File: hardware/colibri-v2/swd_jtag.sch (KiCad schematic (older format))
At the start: 10 parts

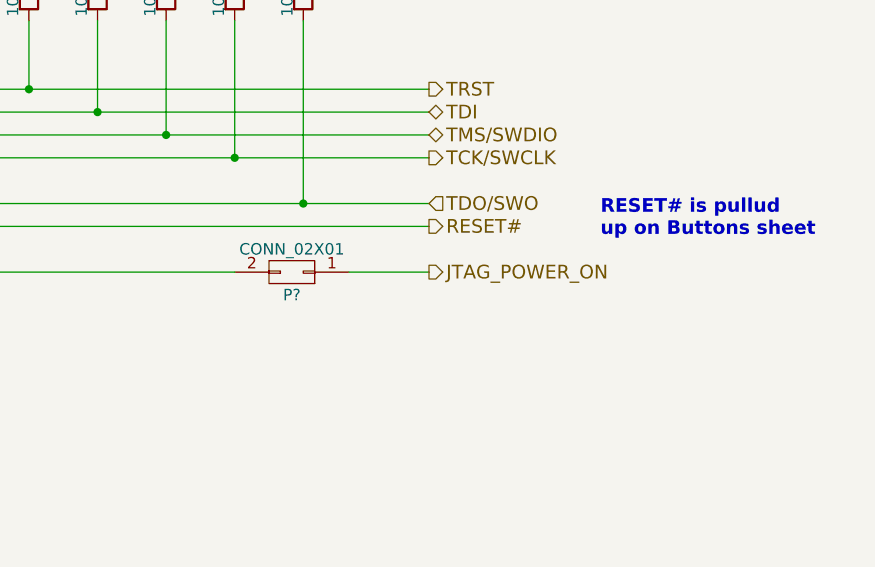
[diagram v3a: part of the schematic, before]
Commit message: Work on cortex,jtag,buttons sheets
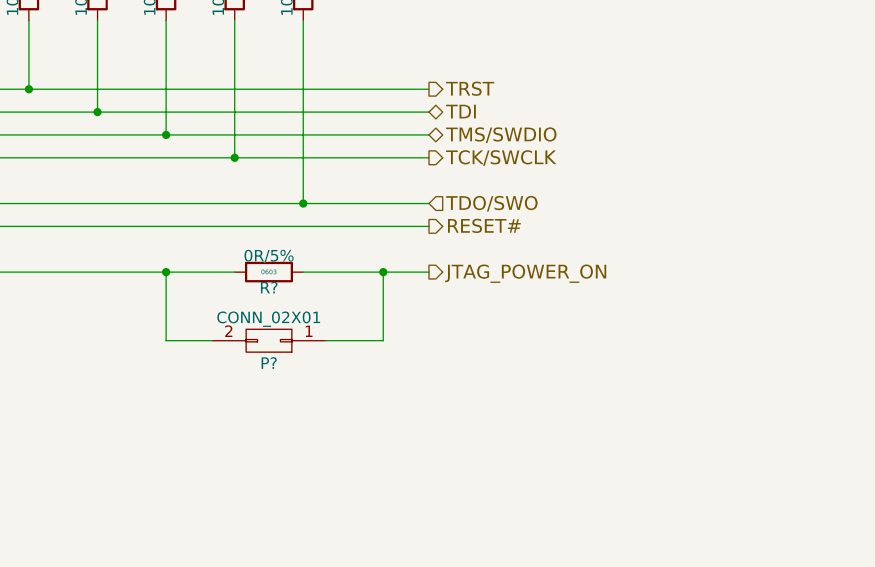
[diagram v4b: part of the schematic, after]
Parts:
- added R?: 0R/5%, Resistors_SMD:R_0603, symbol R_SMT
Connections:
- net JTAG_POWER: now also R?.2
- net JTAG_POWER_ON: now also R?.1
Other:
- note removed: "RESET# is pullud \nup on Buttons sheet"
- moved on the sheet: P?
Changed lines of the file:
@@
 L CONN_02X01 P?
 U 1 1 55768A67
-P 7900 2800
-F 0 "P?" H 7900 2900 50  0000 C CNN
-F 1 "CONN_02X01" H 7900 2700 50  0000 C CNN
-F 2 "" H 7900 1600 60  0001 C CNN
-F 3 "" H 7900 1600 60  0000 C CNN
-	1    7900 2800
+P 7800 3100
+F 0 "P?" H 7800 3200 50  0000 C CNN
+F 1 "CONN_02X01" H 7800 3000 50  0000 C CNN
+F 2 "" H 7800 1900 60  0001 C CNN
+F 3 "" H 7800 1900 60  0000 C CNN
+	1    7800 3100
 	-1   0    0    1
 $EndComp
@@
 	5600 2700 5900 2700
 Wire Wire Line
-	8150 2800 8500 2800
+	7950 2800 8500 2800
 Wire Wire Line
 	3300 1200 7950 1200
@@
 Wire Wire Line
 	4000 5000 4950 5000
-Text Notes 9250 2650 0    60   ~ 12
-RESET# is pullud \nup on Buttons sheet
 Wire Wire Line
 	7650 1700 7650 2300
@@
 	0    1    1    0
 $EndComp
+$Comp
+L R_SMT R?
+U 1 1 56C5EE4B
+P 7800 2800
+F 0 "R?" V 7870 2800 50  0000 C CNN
+F 1 "0R/5%" V 7730 2800 50  0000 C CNN
+F 2 "Resistors_SMD:R_0603" V 7950 2800 30  0001 C CNN
+F 3 "" V 7880 2800 30  0000 C CNN
+F 4 "0603" V 7800 2800 20  0000 C CNN "SMT"
+F 5 "1469739" V 8000 2800 30  0001 C CNN "Part"
+F 6 "Farnell" V 8050 2800 30  0001 C CNN "Provider"
+	1    7800 2800
+	0    1    1    0
+$EndComp
+Wire Wire Line
+	7550 3100 7350 3100
+Wire Wire Line
+	7350 3100 7350 2800
+Connection ~ 7350 2800
+Wire Wire Line
+	8050 3100 8300 3100
+Wire Wire Line
+	8300 3100 8300 2800
+Connection ~ 8300 2800
 $EndSCHEMATC

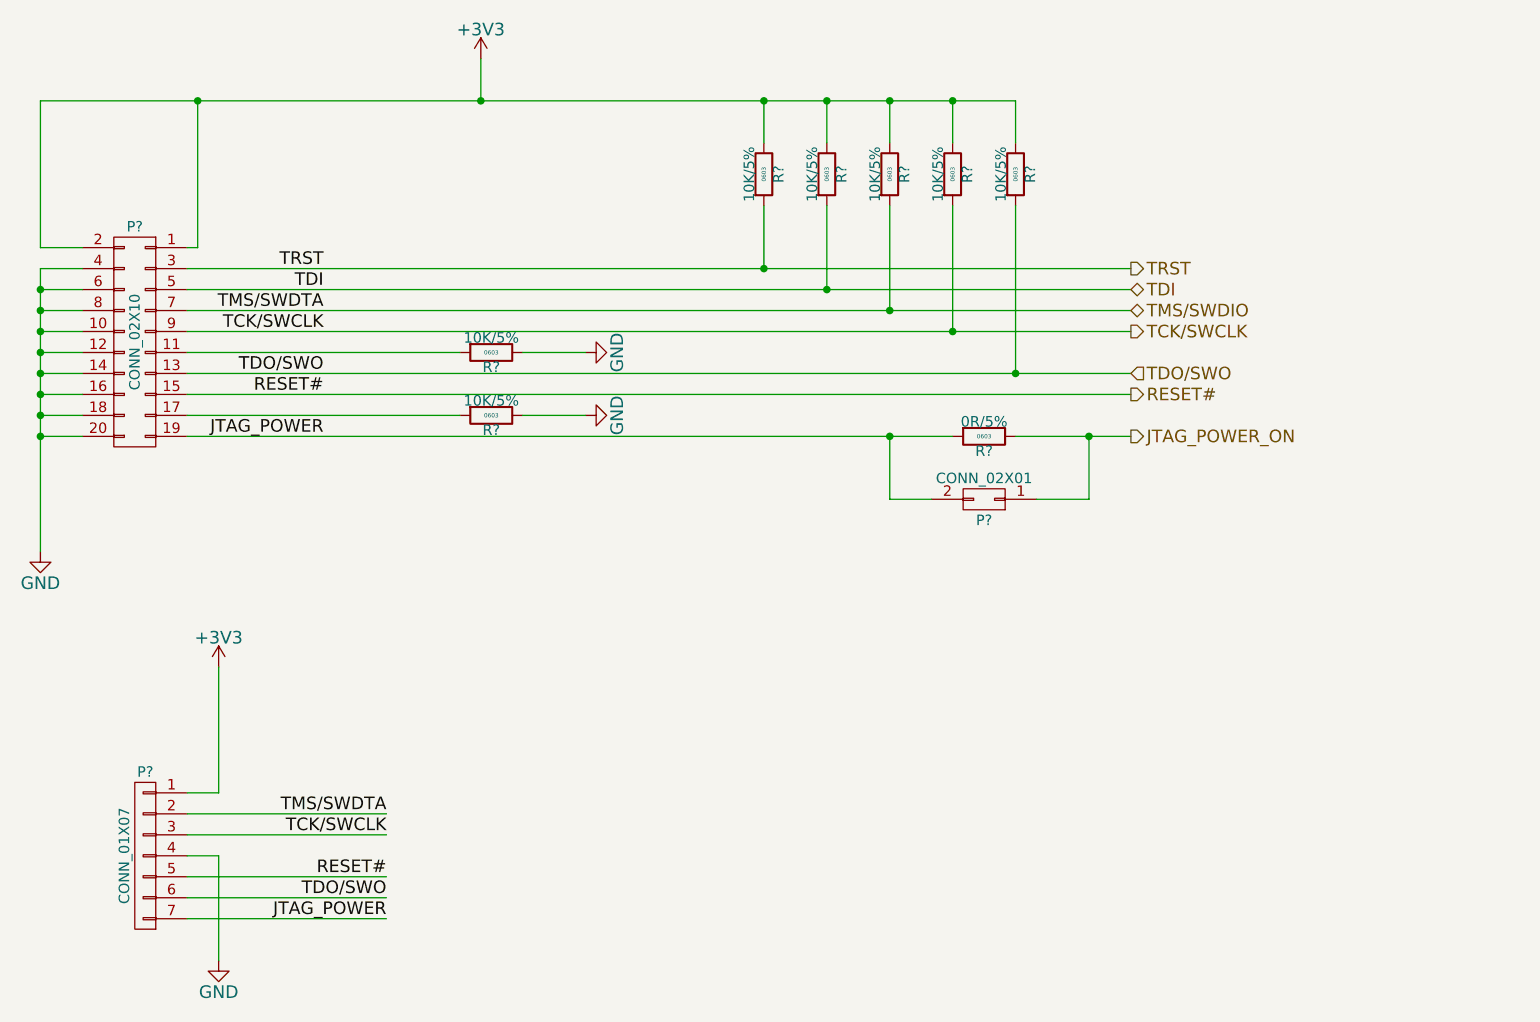
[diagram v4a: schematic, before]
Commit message: Resolving ERC problems
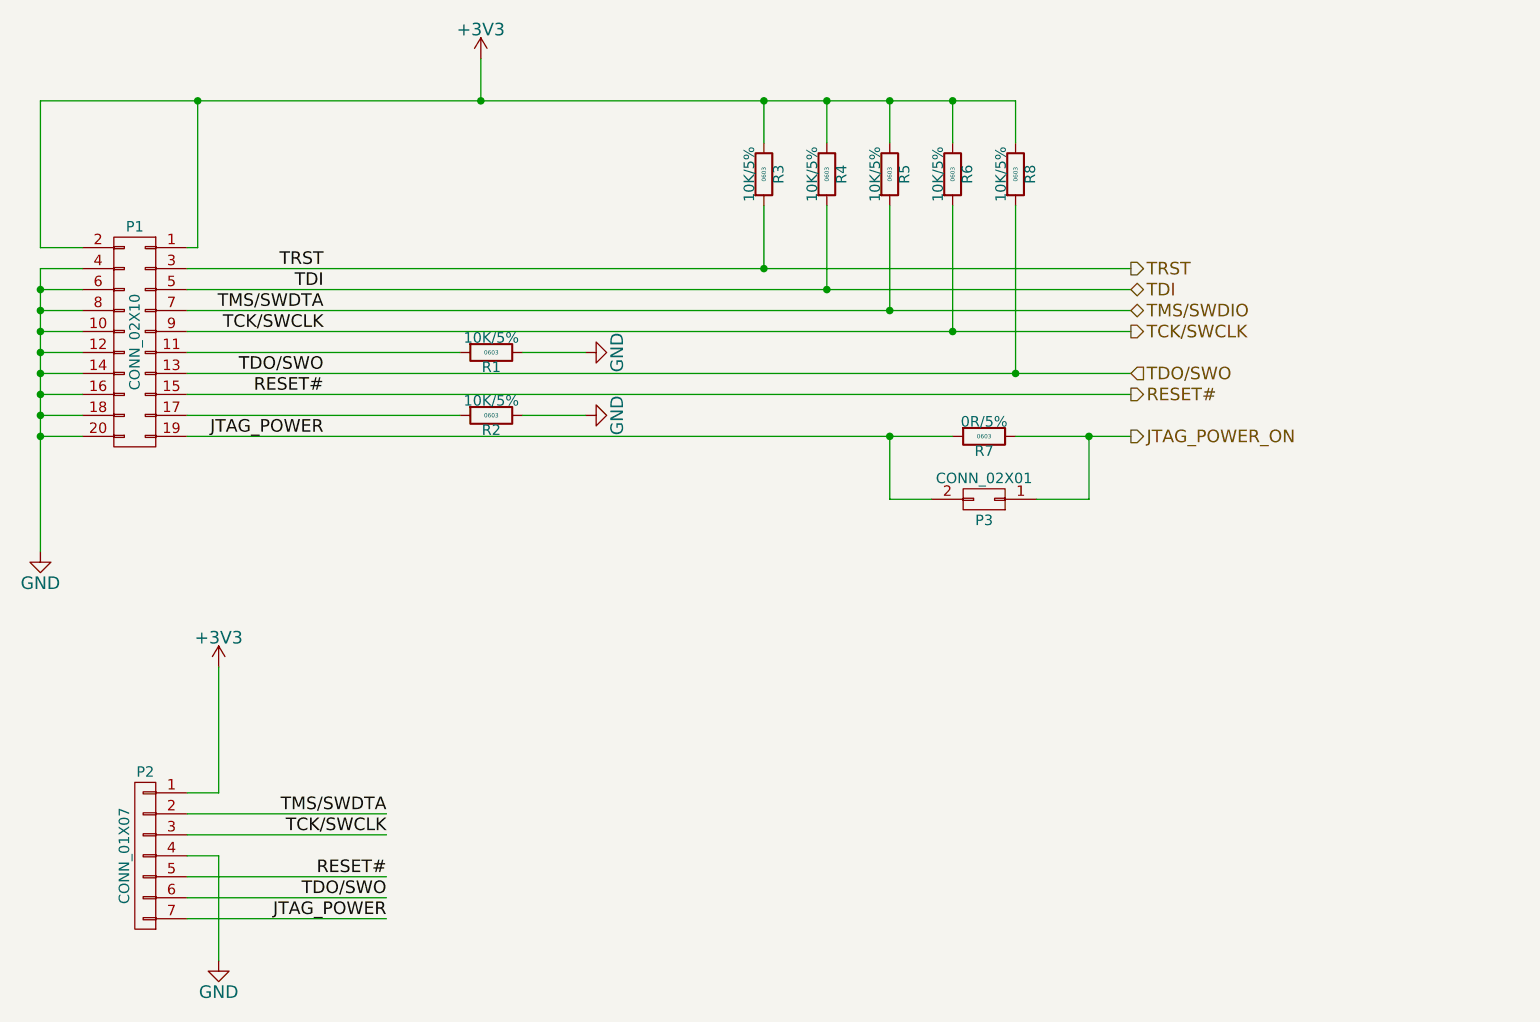
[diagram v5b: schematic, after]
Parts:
- gave numbers to parts that had none: 11
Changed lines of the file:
@@
 EESchema Schematic File Version 2
+LIBS:colibri-wnd-rescue
 LIBS:power
 LIBS:device
@@
 $Descr A4 11693 8268
 encoding utf-8
-Sheet 3 28
+Sheet 2 28
 Title ""
 Date ""
@@
 $EndDescr
 $Comp
-L CONN_02X10 P?
+L CONN_02X10 P1
 U 1 1 55768A13
 P 3750 2350
-F 0 "P?" H 3750 2900 50  0000 C CNN
+F 0 "P1" H 3750 2900 50  0000 C CNN
 F 1 "CONN_02X10" V 3750 2350 50  0000 C CNN
 F 2 "" H 3750 1150 60  0001 C CNN
@@
 $EndComp
 $Comp
-L GND #PWR?
+L GND #PWR01
 U 1 1 55768A1A
 P 3300 3350
-F 0 "#PWR?" H 3300 3100 60  0001 C CNN
+F 0 "#PWR01" H 3300 3100 60  0001 C CNN
 F 1 "GND" H 3300 3200 60  0000 C CNN
 F 2 "" H 3300 3350 60  0000 C CNN
@@
 $EndComp
 $Comp
-L CONN_01X07 P?
+L CONN_01X07 P2
 U 1 1 55768A50
 P 3800 4800
-F 0 "P?" H 3800 5200 50  0000 C CNN
+F 0 "P2" H 3800 5200 50  0000 C CNN
 F 1 "CONN_01X07" V 3900 4800 50  0000 C CNN
 F 2 "" H 3800 4800 60  0001 C CNN
@@
 RESET#
 $Comp
-L GND #PWR?
+L GND #PWR02
 U 1 1 55768A5A
 P 4150 5300
-F 0 "#PWR?" H 4150 5050 60  0001 C CNN
+F 0 "#PWR02" H 4150 5050 60  0001 C CNN
 F 1 "GND" H 4150 5150 60  0000 C CNN
 F 2 "" H 4150 5300 60  0000 C CNN
@@
 $EndComp
 $Comp
-L CONN_02X01 P?
+L CONN_02X01 P3
 U 1 1 55768A67
 P 7800 3100
-F 0 "P?" H 7800 3200 50  0000 C CNN
+F 0 "P3" H 7800 3200 50  0000 C CNN
 F 1 "CONN_02X01" H 7800 3000 50  0000 C CNN
 F 2 "" H 7800 1900 60  0001 C CNN
@@
 $EndComp
 $Comp
-L +3V3 #PWR?
+L +3V3 #PWR03
 U 1 1 55768A6E
 P 4150 3900
-F 0 "#PWR?" H 4150 3750 60  0001 C CNN
+F 0 "#PWR03" H 4150 3750 60  0001 C CNN
 F 1 "+3V3" H 4150 4040 60  0000 C CNN
 F 2 "" H 4150 3900 60  0000 C CNN
@@
 TRST
 $Comp
-L GND #PWR?
+L GND #PWR04
 U 1 1 5576A90F
 P 5900 2400
-F 0 "#PWR?" H 5900 2150 60  0001 C CNN
+F 0 "#PWR04" H 5900 2150 60  0001 C CNN
 F 1 "GND" H 5900 2250 60  0000 C CNN
 F 2 "" H 5900 2400 60  0000 C CNN
@@
 $EndComp
 $Comp
-L GND #PWR?
+L GND #PWR05
 U 1 1 5576A932
 P 5900 2700
-F 0 "#PWR?" H 5900 2450 60  0001 C CNN
+F 0 "#PWR05" H 5900 2450 60  0001 C CNN
 F 1 "GND" H 5900 2550 60  0000 C CNN
 F 2 "" H 5900 2700 60  0000 C CNN
@@
 JTAG_POWER_ON
 $Comp
-L +3V3 #PWR?
+L +3V3 #PWR06
 U 1 1 5576ACC9
 P 5400 1000
-F 0 "#PWR?" H 5400 850 60  0001 C CNN
+F 0 "#PWR06" H 5400 850 60  0001 C CNN
 F 1 "+3V3" H 5400 1140 60  0000 C CNN
 F 2 "" H 5400 1000 60  0000 C CNN
@@
 Connection ~ 6750 2000
 $Comp
-L R_SMT R?
+L R_SMT R1
 U 1 1 56289A38
 P 5450 2400
-F 0 "R?" V 5520 2400 50  0000 C CNN
+F 0 "R1" V 5520 2400 50  0000 C CNN
 F 1 "10K/5%" V 5380 2400 50  0000 C CNN
 F 2 "Resistors_SMD:R_0603" V 5600 2400 30  0001 C CNN
@@
 $EndComp
 $Comp
-L R_SMT R?
+L R_SMT R8
 U 1 1 56289B1A
 P 7950 1550
-F 0 "R?" V 8020 1550 50  0000 C CNN
+F 0 "R8" V 8020 1550 50  0000 C CNN
 F 1 "10K/5%" V 7880 1550 50  0000 C CNN
 F 2 "Resistors_SMD:R_0603" V 8100 1550 30  0001 C CNN
@@
 $EndComp
 $Comp
-L R_SMT R?
+L R_SMT R6
 U 1 1 56289B65
 P 7650 1550
-F 0 "R?" V 7720 1550 50  0000 C CNN
+F 0 "R6" V 7720 1550 50  0000 C CNN
 F 1 "10K/5%" V 7580 1550 50  0000 C CNN
 F 2 "Resistors_SMD:R_0603" V 7800 1550 30  0001 C CNN
@@
 $EndComp
 $Comp
-L R_SMT R?
+L R_SMT R5
 U 1 1 56289B9F
 P 7350 1550
-F 0 "R?" V 7420 1550 50  0000 C CNN
+F 0 "R5" V 7420 1550 50  0000 C CNN
 F 1 "10K/5%" V 7280 1550 50  0000 C CNN
 F 2 "Resistors_SMD:R_0603" V 7500 1550 30  0001 C CNN
@@
 $EndComp
 $Comp
-L R_SMT R?
+L R_SMT R4
 U 1 1 56289BDC
 P 7050 1550
-F 0 "R?" V 7120 1550 50  0000 C CNN
+F 0 "R4" V 7120 1550 50  0000 C CNN
 F 1 "10K/5%" V 6980 1550 50  0000 C CNN
 F 2 "Resistors_SMD:R_0603" V 7200 1550 30  0001 C CNN
@@
 $EndComp
 $Comp
-L R_SMT R?
+L R_SMT R3
 U 1 1 56289C1C
 P 6750 1550
-F 0 "R?" V 6820 1550 50  0000 C CNN
+F 0 "R3" V 6820 1550 50  0000 C CNN
 F 1 "10K/5%" V 6680 1550 50  0000 C CNN
 F 2 "Resistors_SMD:R_0603" V 6900 1550 30  0001 C CNN
@@
 $EndComp
 $Comp
-L R_SMT R?
+L R_SMT R2
 U 1 1 56289D4E
 P 5450 2700
-F 0 "R?" V 5520 2700 50  0000 C CNN
+F 0 "R2" V 5520 2700 50  0000 C CNN
 F 1 "10K/5%" V 5380 2700 50  0000 C CNN
 F 2 "Resistors_SMD:R_0603" V 5600 2700 30  0001 C CNN
@@
 $EndComp
 $Comp
-L R_SMT R?
+L R_SMT R7
 U 1 1 56C5EE4B
 P 7800 2800
-F 0 "R?" V 7870 2800 50  0000 C CNN
+F 0 "R7" V 7870 2800 50  0000 C CNN
 F 1 "0R/5%" V 7730 2800 50  0000 C CNN
 F 2 "Resistors_SMD:R_0603" V 7950 2800 30  0001 C CNN
